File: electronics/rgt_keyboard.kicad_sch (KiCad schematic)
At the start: 61 parts, among them J5 Conn_01x05_Female, J6 Conn_01x05_Male, SW30 SW_SPST, SW31 SW_SPST, SW32 SW_SPST, SW33 SW_SPST, SW34 SW_SPST, SW35 SW_SPST, SW36 SW_SPST, SW37 SW_SPST, SW38 SW_SPST, SW39 SW_SPST, SW40 SW_SPST, SW41 SW_SPST, SW42 SW_SPST, SW43 SW_SPST, SW44 SW_SPST, SW45 SW_SPST, SW46 SW_SPST, SW47 SW_SPST, SW48 SW_SPST, SW49 SW_SPST, SW50 SW_SPST, SW51 SW_SPST, SW52 SW_SPST, SW53 SW_SPST, SW54 SW_SPST, SW55 SW_SPST, SW56 SW_SPST, SW57 SW_SPST, SW58 SW_SPST, U3 PCA9675PW

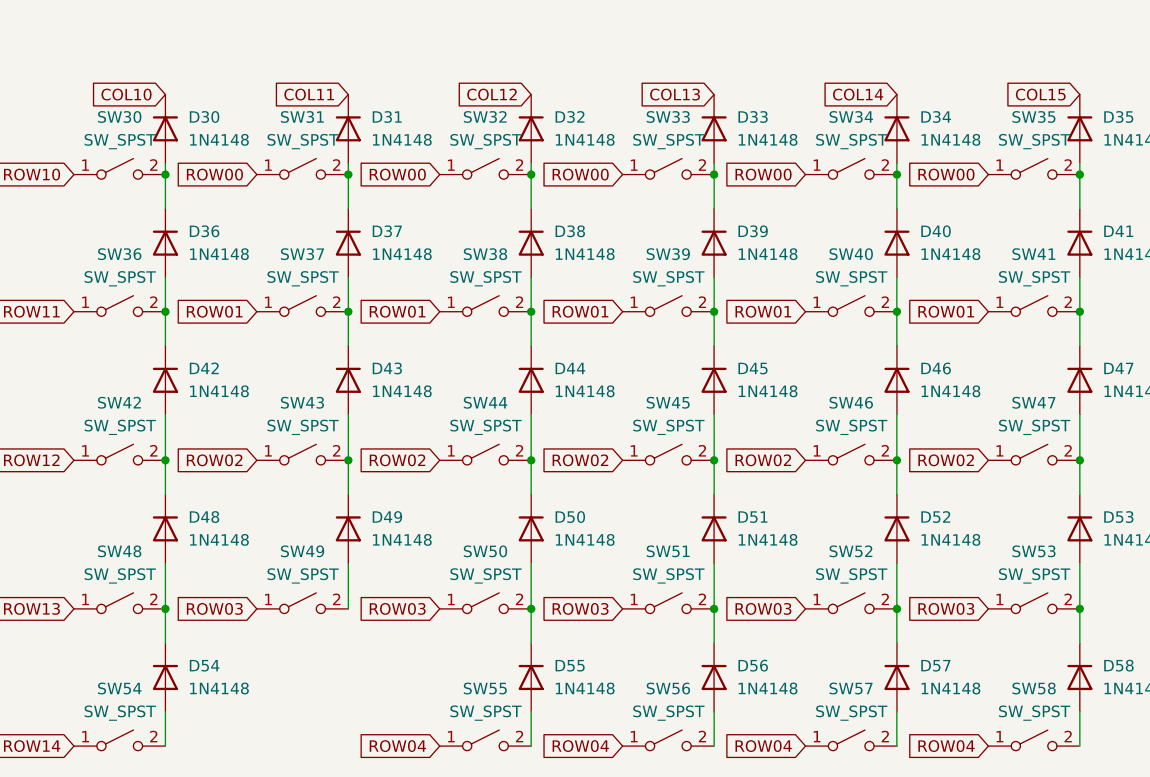
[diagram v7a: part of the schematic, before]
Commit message: fix matrix on right keyboard
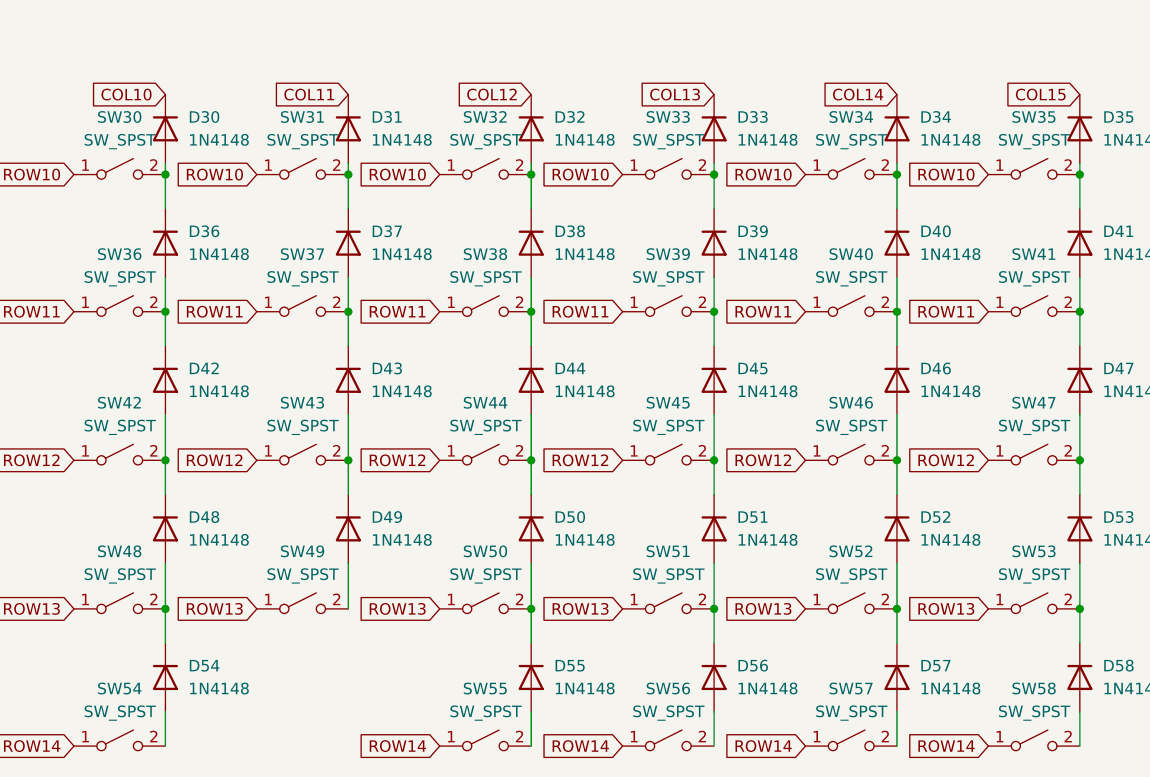
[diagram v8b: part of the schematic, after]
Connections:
- net ROW00 is gone; now on net ROW10: SW31.1 (A), SW32.1 (A), SW33.1 (A), SW34.1 (A), SW35.1 (A)
- net ROW01 is gone; now on net ROW11: SW37.1 (A), SW38.1 (A), SW39.1 (A), SW40.1 (A), SW41.1 (A)
- net ROW02 is gone; now on net ROW12: SW43.1 (A), SW44.1 (A), SW45.1 (A), SW46.1 (A), SW47.1 (A)
- net ROW03 is gone; now on net ROW13: SW49.1 (A), SW50.1 (A), SW51.1 (A), SW52.1 (A), SW53.1 (A)
- net ROW04 is gone; now on net ROW14: SW55.1 (A), SW56.1 (A), SW57.1 (A), SW58.1 (A)
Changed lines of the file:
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@@
     )
   )
-  (global_label "ROW00" (shape input) (at 78.74 92.71 180) (fields_autoplaced)
+  (global_label "ROW10" (shape input) (at 78.74 92.71 180) (fields_autoplaced)
     (effects (font (size 1.27 1.27)) (justify right))
     (property "Intersheet References" "${INTERSHEET_REFS}" (id 0) (at 69.8559 92.6306 0)
@@
     )
   )
-  (global_label "ROW00" (shape input) (at 99.06 92.71 180) (fields_autoplaced)
+  (global_label "ROW10" (shape input) (at 99.06 92.71 180) (fields_autoplaced)
     (effects (font (size 1.27 1.27)) (justify right))
     (property "Intersheet References" "${INTERSHEET_REFS}" (id 0) (at 90.1759 92.6306 0)
@@
     )
   )
-  (global_label "ROW01" (shape input) (at 119.38 107.95 180) (fields_autoplaced)
+  (global_label "ROW11" (shape input) (at 119.38 107.95 180) (fields_autoplaced)
     (effects (font (size 1.27 1.27)) (justify right))
     (property "Intersheet References" "${INTERSHEET_REFS}" (id 0) (at 110.4959 107.8706 0)
@@
     )
   )
-  (global_label "ROW00" (shape input) (at 139.7 92.71 180) (fields_autoplaced)
+  (global_label "ROW10" (shape input) (at 139.7 92.71 180) (fields_autoplaced)
     (effects (font (size 1.27 1.27)) (justify right))
     (property "Intersheet References" "${INTERSHEET_REFS}" (id 0) (at 130.8159 92.6306 0)
@@
     )
   )
-  (global_label "ROW02" (shape input) (at 78.74 124.46 180) (fields_autoplaced)
+  (global_label "ROW12" (shape input) (at 78.74 124.46 180) (fields_autoplaced)
     (effects (font (size 1.27 1.27)) (justify right))
     (property "Intersheet References" "${INTERSHEET_REFS}" (id 0) (at 69.8559 124.3806 0)
@@
     )
   )
-  (global_label "ROW01" (shape input) (at 78.74 107.95 180) (fields_autoplaced)
+  (global_label "ROW11" (shape input) (at 78.74 107.95 180) (fields_autoplaced)
     (effects (font (size 1.27 1.27)) (justify right))
     (property "Intersheet References" "${INTERSHEET_REFS}" (id 0) (at 69.8559 107.8706 0)
@@
     )
   )
-  (global_label "ROW00" (shape input) (at 58.42 92.71 180) (fields_autoplaced)
+  (global_label "ROW10" (shape input) (at 58.42 92.71 180) (fields_autoplaced)
     (effects (font (size 1.27 1.27)) (justify right))
     (property "Intersheet References" "${INTERSHEET_REFS}" (id 0) (at 49.5359 92.6306 0)
@@
     )
   )
-  (global_label "ROW02" (shape input) (at 119.38 124.46 180) (fields_autoplaced)
+  (global_label "ROW12" (shape input) (at 119.38 124.46 180) (fields_autoplaced)
     (effects (font (size 1.27 1.27)) (justify right))
     (property "Intersheet References" "${INTERSHEET_REFS}" (id 0) (at 110.4959 124.3806 0)
@@
     )
   )
-  (global_label "ROW04" (shape input) (at 78.74 156.21 180) (fields_autoplaced)
+  (global_label "ROW14" (shape input) (at 78.74 156.21 180) (fields_autoplaced)
     (effects (font (size 1.27 1.27)) (justify right))
     (property "Intersheet References" "${INTERSHEET_REFS}" (id 0) (at 69.8559 156.1306 0)
@@
     )
   )
-  (global_label "ROW01" (shape input) (at 58.42 107.95 180) (fields_autoplaced)
+  (global_label "ROW11" (shape input) (at 58.42 107.95 180) (fields_autoplaced)
     (effects (font (size 1.27 1.27)) (justify right))
     (property "Intersheet References" "${INTERSHEET_REFS}" (id 0) (at 49.5359 107.8706 0)
@@
     )
   )
-  (global_label "ROW01" (shape input) (at 139.7 107.95 180) (fields_autoplaced)
+  (global_label "ROW11" (shape input) (at 139.7 107.95 180) (fields_autoplaced)
     (effects (font (size 1.27 1.27)) (justify right))
     (property "Intersheet References" "${INTERSHEET_REFS}" (id 0) (at 130.8159 107.8706 0)
@@
     )
   )
-  (global_label "ROW04" (shape input) (at 139.7 156.21 180) (fields_autoplaced)
+  (global_label "ROW14" (shape input) (at 139.7 156.21 180) (fields_autoplaced)
     (effects (font (size 1.27 1.27)) (justify right))
     (property "Intersheet References" "${INTERSHEET_REFS}" (id 0) (at 130.8159 156.1306 0)
@@
     )
   )
-  (global_label "ROW03" (shape input) (at 119.38 140.97 180) (fields_autoplaced)
+  (global_label "ROW13" (shape input) (at 119.38 140.97 180) (fields_autoplaced)
     (effects (font (size 1.27 1.27)) (justify right))
     (property "Intersheet References" "${INTERSHEET_REFS}" (id 0) (at 110.4959 140.8906 0)
@@
     )
   )
-  (global_label "ROW02" (shape input) (at 99.06 124.46 180) (fields_autoplaced)
+  (global_label "ROW12" (shape input) (at 99.06 124.46 180) (fields_autoplaced)
     (effects (font (size 1.27 1.27)) (justify right))
     (property "Intersheet References" "${INTERSHEET_REFS}" (id 0) (at 90.1759 124.3806 0)
@@
     )
   )
-  (global_label "ROW01" (shape input) (at 99.06 107.95 180) (fields_autoplaced)
+  (global_label "ROW11" (shape input) (at 99.06 107.95 180) (fields_autoplaced)
     (effects (font (size 1.27 1.27)) (justify right))
     (property "Intersheet References" "${INTERSHEET_REFS}" (id 0) (at 90.1759 107.8706 0)
@@
     )
   )
-  (global_label "ROW04" (shape input) (at 99.06 156.21 180) (fields_autoplaced)
+  (global_label "ROW14" (shape input) (at 99.06 156.21 180) (fields_autoplaced)
     (effects (font (size 1.27 1.27)) (justify right))
     (property "Intersheet References" "${INTERSHEET_REFS}" (id 0) (at 90.1759 156.1306 0)
@@
     )
   )
-  (global_label "ROW03" (shape input) (at 99.06 140.97 180) (fields_autoplaced)
+  (global_label "ROW13" (shape input) (at 99.06 140.97 180) (fields_autoplaced)
     (effects (font (size 1.27 1.27)) (justify right))
     (property "Intersheet References" "${INTERSHEET_REFS}" (id 0) (at 90.1759 140.8906 0)
@@
     )
   )
-  (global_label "ROW03" (shape input) (at 139.7 140.97 180) (fields_autoplaced)
+  (global_label "ROW13" (shape input) (at 139.7 140.97 180) (fields_autoplaced)
     (effects (font (size 1.27 1.27)) (justify right))
     (property "Intersheet References" "${INTERSHEET_REFS}" (id 0) (at 130.8159 140.8906 0)
@@
     )
   )
-  (global_label "ROW03" (shape input) (at 58.42 140.97 180) (fields_autoplaced)
+  (global_label "ROW13" (shape input) (at 58.42 140.97 180) (fields_autoplaced)
     (effects (font (size 1.27 1.27)) (justify right))
     (property "Intersheet References" "${INTERSHEET_REFS}" (id 0) (at 49.5359 140.8906 0)
@@
     )
   )
-  (global_label "ROW04" (shape input) (at 119.38 156.21 180) (fields_autoplaced)
+  (global_label "ROW14" (shape input) (at 119.38 156.21 180) (fields_autoplaced)
     (effects (font (size 1.27 1.27)) (justify right))
     (property "Intersheet References" "${INTERSHEET_REFS}" (id 0) (at 110.4959 156.1306 0)
@@
     )
   )
-  (global_label "ROW00" (shape input) (at 119.38 92.71 180) (fields_autoplaced)
+  (global_label "ROW10" (shape input) (at 119.38 92.71 180) (fields_autoplaced)
     (effects (font (size 1.27 1.27)) (justify right))
     (property "Intersheet References" "${INTERSHEET_REFS}" (id 0) (at 110.4959 92.6306 0)
@@
     )
   )
-  (global_label "ROW02" (shape input) (at 139.7 124.46 180) (fields_autoplaced)
+  (global_label "ROW12" (shape input) (at 139.7 124.46 180) (fields_autoplaced)
     (effects (font (size 1.27 1.27)) (justify right))
     (property "Intersheet References" "${INTERSHEET_REFS}" (id 0) (at 130.8159 124.3806 0)
@@
     )
   )
-  (global_label "ROW02" (shape input) (at 58.42 124.46 180) (fields_autoplaced)
+  (global_label "ROW12" (shape input) (at 58.42 124.46 180) (fields_autoplaced)
     (effects (font (size 1.27 1.27)) (justify right))
     (property "Intersheet References" "${INTERSHEET_REFS}" (id 0) (at 49.5359 124.3806 0)
@@
     )
   )
-  (global_label "ROW03" (shape input) (at 78.74 140.97 180) (fields_autoplaced)
+  (global_label "ROW13" (shape input) (at 78.74 140.97 180) (fields_autoplaced)
     (effects (font (size 1.27 1.27)) (justify right))
     (property "Intersheet References" "${INTERSHEET_REFS}" (id 0) (at 69.8559 140.8906 0)
